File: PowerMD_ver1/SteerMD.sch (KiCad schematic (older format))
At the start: 216 parts, among them P1 SWD, P10 OUT_1, P11 ENC_0, P13 ENC_1, P14 I/O_1, P15 OUT_0, P2 MOTOR_COOLING, P3 CAN, P4 CAN, P5 SERIAL, P6 I/O_0, P7 FAN, P8 BATT_IN, P9 BATT_IN, Q1 MOSFET_N, Q2 MOSFET_N, Q3 MOSFET_N, Q4 MOSFET_N, Q5 MOSFET_N, Q6 MOSFET_N, Q7 MOSFET_N, Q8 MOSFET_N, SW1 RST, SW3 SW0, SW4 SW1, U1 MAX3051, U10 ACS758, U11 POWER_ON, U12 SI8274, U13 ACS758, U14 SI8274, U15 AZ1086H, U16 LOGO, U17 AQM0802, U19 ADRESS, U2 BD9G101, U3 STM32F405RG, U4 SI8274, U5 SI8900, U6 ADC_~RST, U7 BD9G101G, U8 SI8274, U9 BD33FA1, Y1 8MHz

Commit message: 途中
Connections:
- net +BATT: now also Q1.D, Q3.D, Q5.D, Q7.D; no longer U10.4 (IP+), U13.4 (IP+)
- net GNDPWR: now also U10.5 (IP-), U13.5 (IP-); no longer C20.2, C31.2, C46.2, C49.2, Q2.S, Q4.S, Q6.S, Q8.S, U12.9 (GNCB), U14.9 (GNCB), U4.9 (GNCB), U8.9 (GNCB)
- net MOTOR0_BATT: now also C20.2, C31.2, Q2.S, Q6.S, U10.4 (IP+), U12.9 (GNCB), U4.9 (GNCB); no longer Q1.D, Q5.D, U10.5 (IP-)
- net MOTOR1_BATT: now also C46.2, C49.2, Q4.S, Q8.S, U13.4 (IP+), U14.9 (GNCB), U8.9 (GNCB); no longer Q3.D, Q7.D, U13.5 (IP-)
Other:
- moved on the sheet: C18, C19, C20, C21, C23, C25, C28, C29, C30, C31, C32, C36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

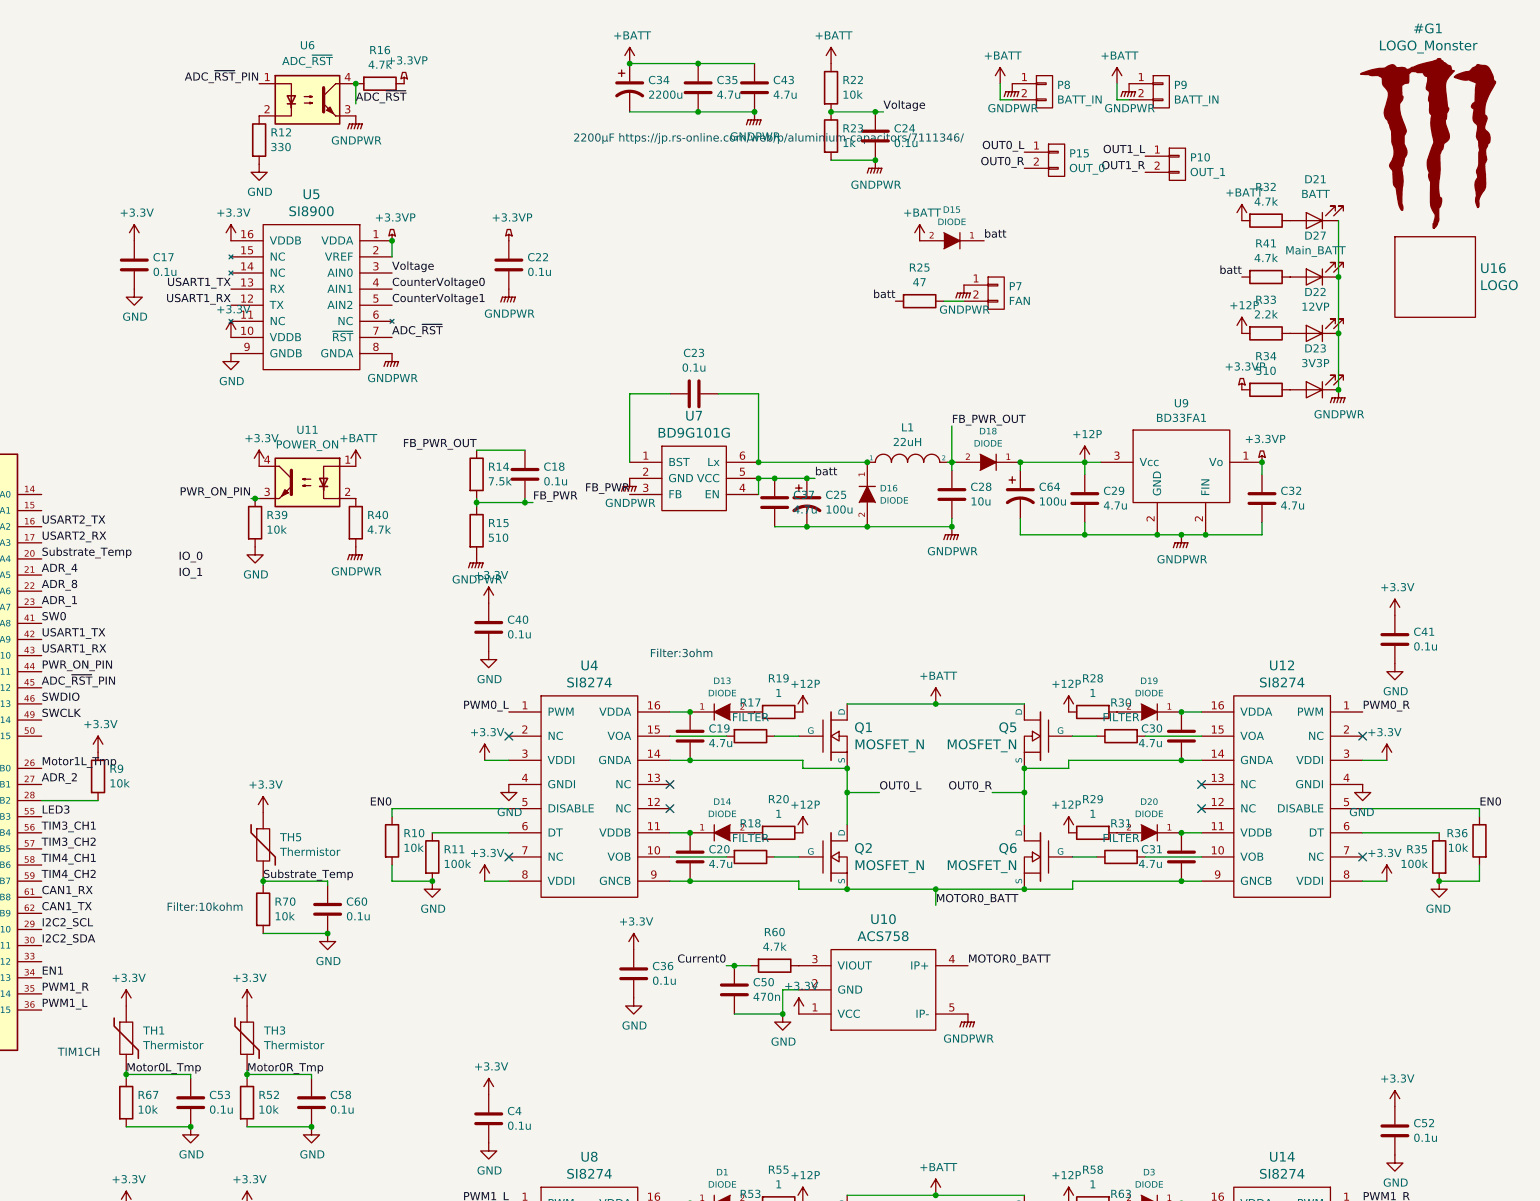
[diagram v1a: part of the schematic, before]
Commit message: Power MD 電流センシングをローサイドでセンシングするように変更した&DAC乗っけた
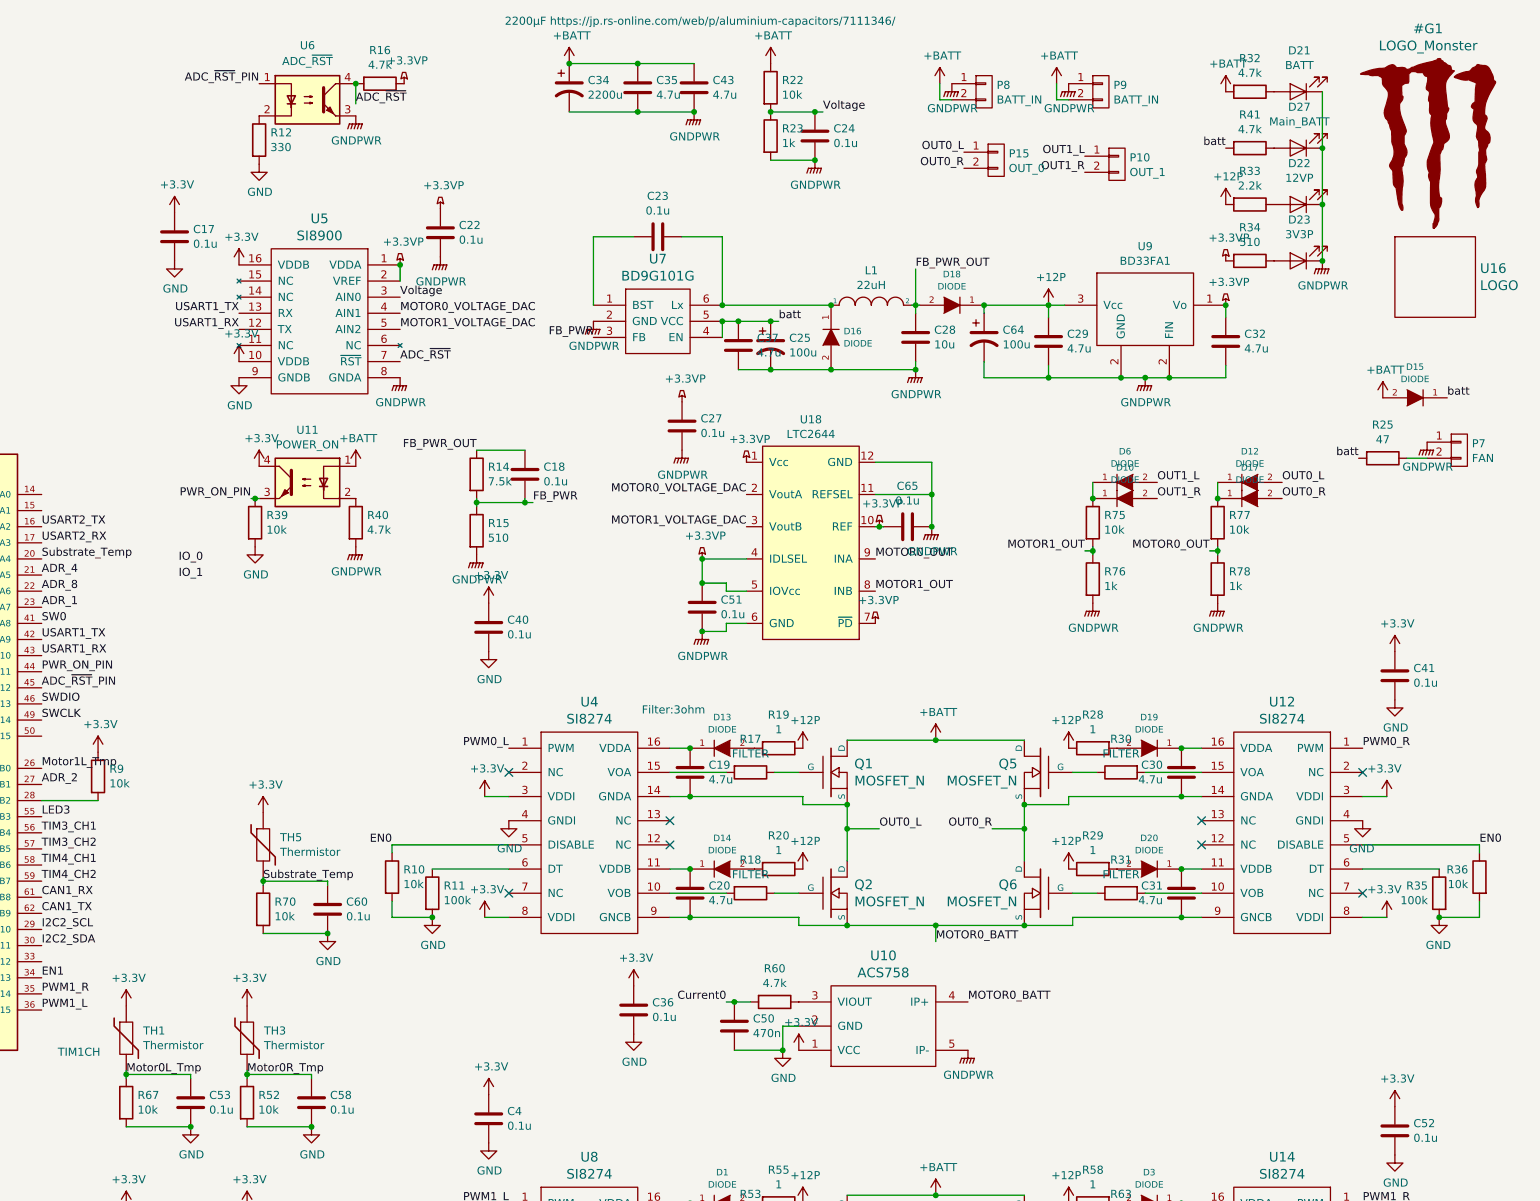
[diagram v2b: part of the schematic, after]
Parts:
- added C27, C51: 0.1u, Mizz_lib:1608_WP, symbol SteerMD-rescue:C-Device-MD_Enbarr_x2-rescue-F4_CAN_DCMD-rescue
- added C65: 0.1u, Capacitor_SMD:C_0603_1608Metric, symbol SteerMD-rescue:C-Device-MD_Enbarr_x2-rescue-F4_CAN_DCMD-rescue
- added D10, D12, D17, D6: DIODE, Mizz_lib:1608_WP, symbol SteerMD-rescue:DIODE-device-MD_Enbarr_x2-rescue-F4_CAN_DCMD-rescue
- added R75, R77: 10k, Resistor_SMD:R_0603_1608Metric, symbol SteerMD-rescue:R-Device-MD_Enbarr_x2-rescue-F4_CAN_DCMD-rescue
- added R76, R78: 1k, Resistor_SMD:R_0603_1608Metric, symbol SteerMD-rescue:R-Device-MD_Enbarr_x2-rescue-F4_CAN_DCMD-rescue
- added U18: LTC2644, Package_SO:MSOP-12_3x4mm_P0.65mm, symbol Miz:LTC2644
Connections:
- net +3.3VP: now also C27.1, C51.1, C65.2, U18.1 (Vcc), U18.10 (REF), U18.4 (IDLSEL), U18.5 (IOVcc), U18.7 (~PD)
- net GNDPWR: now also C27.2, C51.2, C65.1, R76.2, R78.2, U18.11 (REFSEL), U18.12 (GND), U18.6 (GND)
- net OUT0_L: now also D12.2 (A)
- net OUT0_R: now also D17.2 (A)
- net OUT1_L: now also D6.2 (A)
- net OUT1_R: now also D10.2 (A)
- net CounterVoltage0 renamed MOTOR0_VOLTAGE_DAC
- net MOTOR0_VOLTAGE_DAC: now also U18.2 (VoutA)
- net CounterVoltage1 renamed MOTOR1_VOLTAGE_DAC
- net MOTOR1_VOLTAGE_DAC: now also U18.3 (VoutB)
- new net: D12.1 (K), D17.1 (K), R77.1
- new net: D10.1 (K), D6.1 (K), R75.1
- new net MOTOR0_OUT: R77.2, R78.1, U18.9 (INA)
- new net MOTOR1_OUT: R75.2, R76.1, U18.8 (INB)
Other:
- note removed: "Filter:10kohm"
- moved on the sheet: C17, C19, C20, C22, C23, C24, C25, C28, C29, C30, C31, C32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

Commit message: ブラシレス復元の続き
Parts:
- R17, R18, R30, R31, R53, R54, R63, R64: footprint Resistor_SMD:R_0603_1608Metric -> Mizz_lib:1608_WP
- TH1, TH2, TH3, TH4: footprint Capacitor_SMD:C_0603_1608Metric -> Mizz_lib:1608_WP
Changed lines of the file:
@@
 F 0 "TH1" H 7530 6871 50  0000 L CNN
 F 1 "Thermistor" H 7530 6780 50  0000 L CNN
-F 2 "Capacitor_SMD:C_0603_1608Metric" H 7425 6825 50  0001 C CNN
+F 2 "Mizz_lib:1608_WP" H 7425 6825 50  0001 C CNN
 F 3 "~" H 7425 6825 50  0001 C CNN
 	1    7425 6825
@@
 F 0 "TH2" H 7530 8121 50  0000 L CNN
 F 1 "Thermistor" H 7530 8030 50  0000 L CNN
-F 2 "Capacitor_SMD:C_0603_1608Metric" H 7425 8075 50  0001 C CNN
+F 2 "Mizz_lib:1608_WP" H 7425 8075 50  0001 C CNN
 F 3 "~" H 7425 8075 50  0001 C CNN
 	1    7425 8075
@@
 F 0 "TH3" H 8280 6871 50  0000 L CNN
 F 1 "Thermistor" H 8280 6780 50  0000 L CNN
-F 2 "Capacitor_SMD:C_0603_1608Metric" H 8175 6825 50  0001 C CNN
+F 2 "Mizz_lib:1608_WP" H 8175 6825 50  0001 C CNN
 F 3 "~" H 8175 6825 50  0001 C CNN
 	1    8175 6825
@@
 F 0 "TH4" H 8280 8121 50  0000 L CNN
 F 1 "Thermistor" H 8280 8030 50  0000 L CNN
-F 2 "Capacitor_SMD:C_0603_1608Metric" H 8175 8075 50  0001 C CNN
+F 2 "Mizz_lib:1608_WP" H 8175 8075 50  0001 C CNN
 F 3 "~" H 8175 8075 50  0001 C CNN
 	1    8175 8075
@@
 F 0 "R64" V 13393 8750 50  0000 C CNN
 F 1 "FILTER" V 13484 8750 50  0000 C CNN
-F 2 "Resistor_SMD:R_0603_1608Metric" V 13530 8750 50  0001 C CNN
+F 2 "Mizz_lib:1608_WP" V 13530 8750 50  0001 C CNN
 F 3 "~" H 13600 8750 50  0001 C CNN
 	1    13600 8750
@@
 F 0 "R63" V 13393 8000 50  0000 C CNN
 F 1 "FILTER" V 13484 8000 50  0000 C CNN
-F 2 "Resistor_SMD:R_0603_1608Metric" V 13530 8000 50  0001 C CNN
+F 2 "Mizz_lib:1608_WP" V 13530 8000 50  0001 C CNN
 F 3 "~" H 13600 8000 50  0001 C CNN
 	1    13600 8000
@@
 F 0 "R54" V 11093 8750 50  0000 C CNN
 F 1 "FILTER" V 11184 8750 50  0000 C CNN
-F 2 "Resistor_SMD:R_0603_1608Metric" V 11230 8750 50  0001 C CNN
+F 2 "Mizz_lib:1608_WP" V 11230 8750 50  0001 C CNN
 F 3 "~" H 11300 8750 50  0001 C CNN
 	1    11300 8750
@@
 F 0 "R53" V 11093 8000 50  0000 C CNN
 F 1 "FILTER" V 11184 8000 50  0000 C CNN
-F 2 "Resistor_SMD:R_0603_1608Metric" V 11230 8000 50  0001 C CNN
+F 2 "Mizz_lib:1608_WP" V 11230 8000 50  0001 C CNN
 F 3 "~" H 11300 8000 50  0001 C CNN
 	1    11300 8000
@@
 F 0 "R31" V 13393 5925 50  0000 C CNN
 F 1 "FILTER" V 13484 5925 50  0000 C CNN
-F 2 "Resistor_SMD:R_0603_1608Metric" V 13530 5925 50  0001 C CNN
+F 2 "Mizz_lib:1608_WP" V 13530 5925 50  0001 C CNN
 F 3 "~" H 13600 5925 50  0001 C CNN
 	1    13600 5925
@@
 F 0 "R30" V 13393 5175 50  0000 C CNN
 F 1 "FILTER" V 13484 5175 50  0000 C CNN
-F 2 "Resistor_SMD:R_0603_1608Metric" V 13530 5175 50  0001 C CNN
+F 2 "Mizz_lib:1608_WP" V 13530 5175 50  0001 C CNN
 F 3 "~" H 13600 5175 50  0001 C CNN
 	1    13600 5175
@@
 F 0 "R18" V 11093 5925 50  0000 C CNN
 F 1 "FILTER" V 11184 5925 50  0000 C CNN
-F 2 "Resistor_SMD:R_0603_1608Metric" V 11230 5925 50  0001 C CNN
+F 2 "Mizz_lib:1608_WP" V 11230 5925 50  0001 C CNN
 F 3 "~" H 11300 5925 50  0001 C CNN
 	1    11300 5925
@@
 F 0 "R17" V 11093 5175 50  0000 C CNN
 F 1 "FILTER" V 11184 5175 50  0000 C CNN
-F 2 "Resistor_SMD:R_0603_1608Metric" V 11230 5175 50  0001 C CNN
+F 2 "Mizz_lib:1608_WP" V 11230 5175 50  0001 C CNN
 F 3 "~" H 11300 5175 50  0001 C CNN
 	1    11300 5175
